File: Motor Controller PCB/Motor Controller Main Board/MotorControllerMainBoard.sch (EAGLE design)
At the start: 54 parts, among them T1 TEENSY_3.1_ALL_PINS, U1 TL072CDT

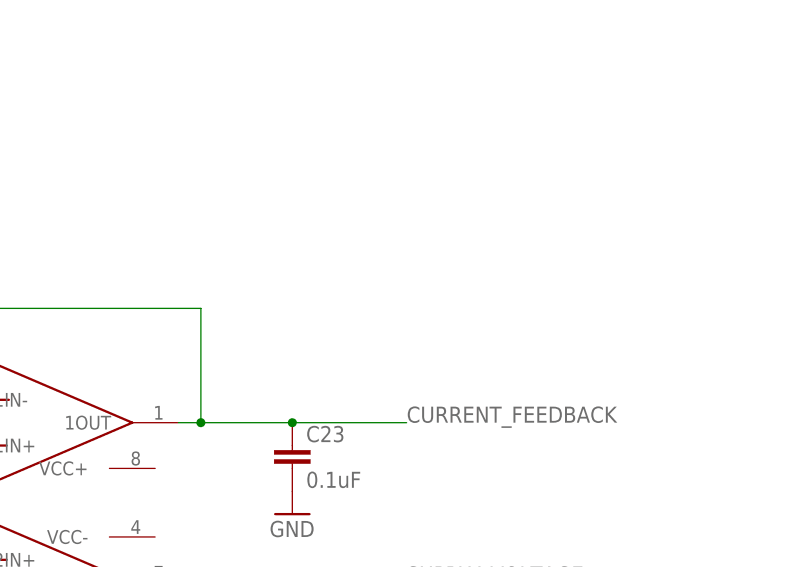
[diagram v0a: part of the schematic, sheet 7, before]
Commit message: Decided to use a different op-amp
A tad more expensive but this new op-amp selection offers little to no
current or voltage offset voltages.
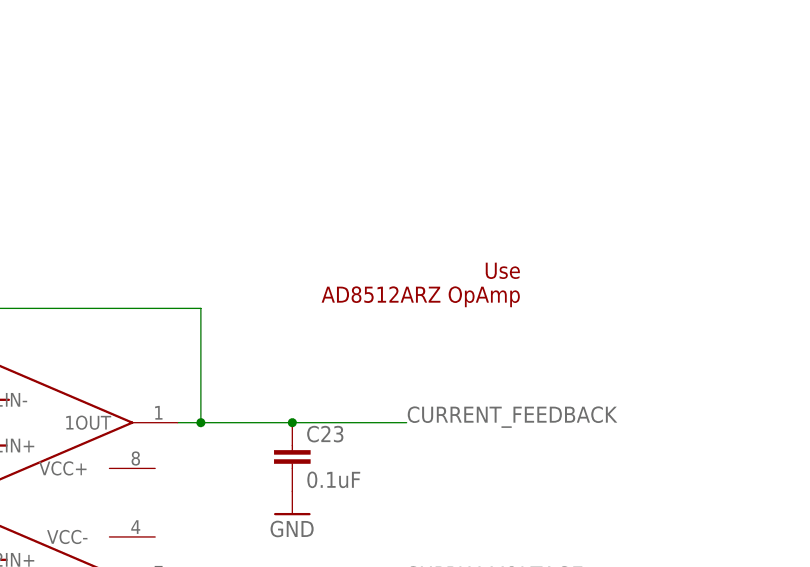
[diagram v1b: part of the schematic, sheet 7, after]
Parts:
- renumbered U1 to AD8512ARZ
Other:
- note added: "Use AD8512ARZ OpAmp"
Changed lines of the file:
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@@
 <part name="R4" library="SparkFun-Passives" deviceset="RESISTOR" device="0805-RES" value="3.3k"/>
 <part name="L1" library="SparkFun (2015_10_14 22_27_04 UTC)" deviceset="INDUCTOR" device="0805" value="42nH"/>
-<part name="U1" library="MotorControllerEagleLibrary" deviceset="TL072CDT" device=""/>
+<part name="AD8512ARZ" library="MotorControllerEagleLibrary" deviceset="TL072CDT" device=""/>
 <part name="C23" library="rcl" deviceset="C-EU" device="C0805" value="0.1uF"/>
 <part name="C24" library="rcl" deviceset="C-EU" device="C0805"/>
@@
 CONNECTIONS</text>
 <text x="195.58" y="43.18" size="1.778" layer="91">2OUT = (R7+R8)/(R5+R6)Vin =~ 1/10*Vin</text>
+<text x="238.76" y="96.52" size="1.778" layer="94" rot="R180">Use
+AD8512ARZ OpAmp
+</text>
 </plain>
 <instances>
@@
 <instance part="R3" gate="G$1" x="43.18" y="50.8" rot="R90"/>
 <instance part="R4" gate="G$1" x="83.82" y="50.8" rot="R90"/>
-<instance part="U1" gate="A" x="190.5" y="68.58"/>
+<instance part="AD8512ARZ" gate="A" x="190.5" y="68.58"/>
 <instance part="C23" gate="G$1" x="213.36" y="76.2"/>
 <instance part="C24" gate="G$1" x="294.64" y="76.2"/>
@@
 </segment>
 <segment>
-<pinref part="U1" gate="A" pin="1IN-"/>
+<pinref part="AD8512ARZ" gate="A" pin="1IN-"/>
 <wire x1="172.72" y1="81.28" x2="167.64" y2="81.28" width="0.1524" layer="91"/>
 <wire x1="167.64" y1="81.28" x2="167.64" y2="91.44" width="0.1524" layer="91"/>
 <wire x1="167.64" y1="91.44" x2="203.2" y2="91.44" width="0.1524" layer="91"/>
 <wire x1="203.2" y1="91.44" x2="203.2" y2="78.74" width="0.1524" layer="91"/>
-<pinref part="U1" gate="A" pin="1OUT"/>
+<pinref part="AD8512ARZ" gate="A" pin="1OUT"/>
 <wire x1="203.2" y1="78.74" x2="200.66" y2="78.74" width="0.1524" layer="91"/>
 <wire x1="203.2" y1="78.74" x2="213.36" y2="78.74" width="0.1524" layer="91"/>
@@
 <net name="CURRENT_SENSOR_OUTPUT" class="0">
 <segment>
-<pinref part="U1" gate="A" pin="1IN+"/>
+<pinref part="AD8512ARZ" gate="A" pin="1IN+"/>
 <wire x1="172.72" y1="76.2" x2="160.02" y2="76.2" width="0.1524" layer="91"/>
 <label x="142.24" y="76.2" size="1.778" layer="95"/>
@@
 <segment>
 <pinref part="R5" gate="G$1" pin="2"/>
-<pinref part="U1" gate="A" pin="2IN+"/>
+<pinref part="AD8512ARZ" gate="A" pin="2IN+"/>
 <wire x1="160.02" y1="66.04" x2="165.1" y2="63.5" width="0.1524" layer="91"/>
 <pinref part="R8" gate="G$1" pin="2"/>
@@
 <segment>
 <pinref part="R6" gate="G$1" pin="2"/>
-<pinref part="U1" gate="A" pin="2IN-"/>
+<pinref part="AD8512ARZ" gate="A" pin="2IN-"/>
 <wire x1="160.02" y1="55.88" x2="170.18" y2="58.42" width="0.1524" layer="91"/>
 <wire x1="170.18" y1="58.42" x2="172.72" y2="58.42" width="0.1524" layer="91"/>
@@
 <wire x1="187.96" y1="48.26" x2="203.2" y2="48.26" width="0.1524" layer="91"/>
 <wire x1="203.2" y1="48.26" x2="203.2" y2="60.96" width="0.1524" layer="91"/>
-<pinref part="U1" gate="A" pin="2OUT"/>
+<pinref part="AD8512ARZ" gate="A" pin="2OUT"/>
 <wire x1="203.2" y1="60.96" x2="200.66" y2="60.96" width="0.1524" layer="91"/>
 <wire x1="203.2" y1="60.96" x2="213.36" y2="60.96" width="0.1524" layer="91"/>

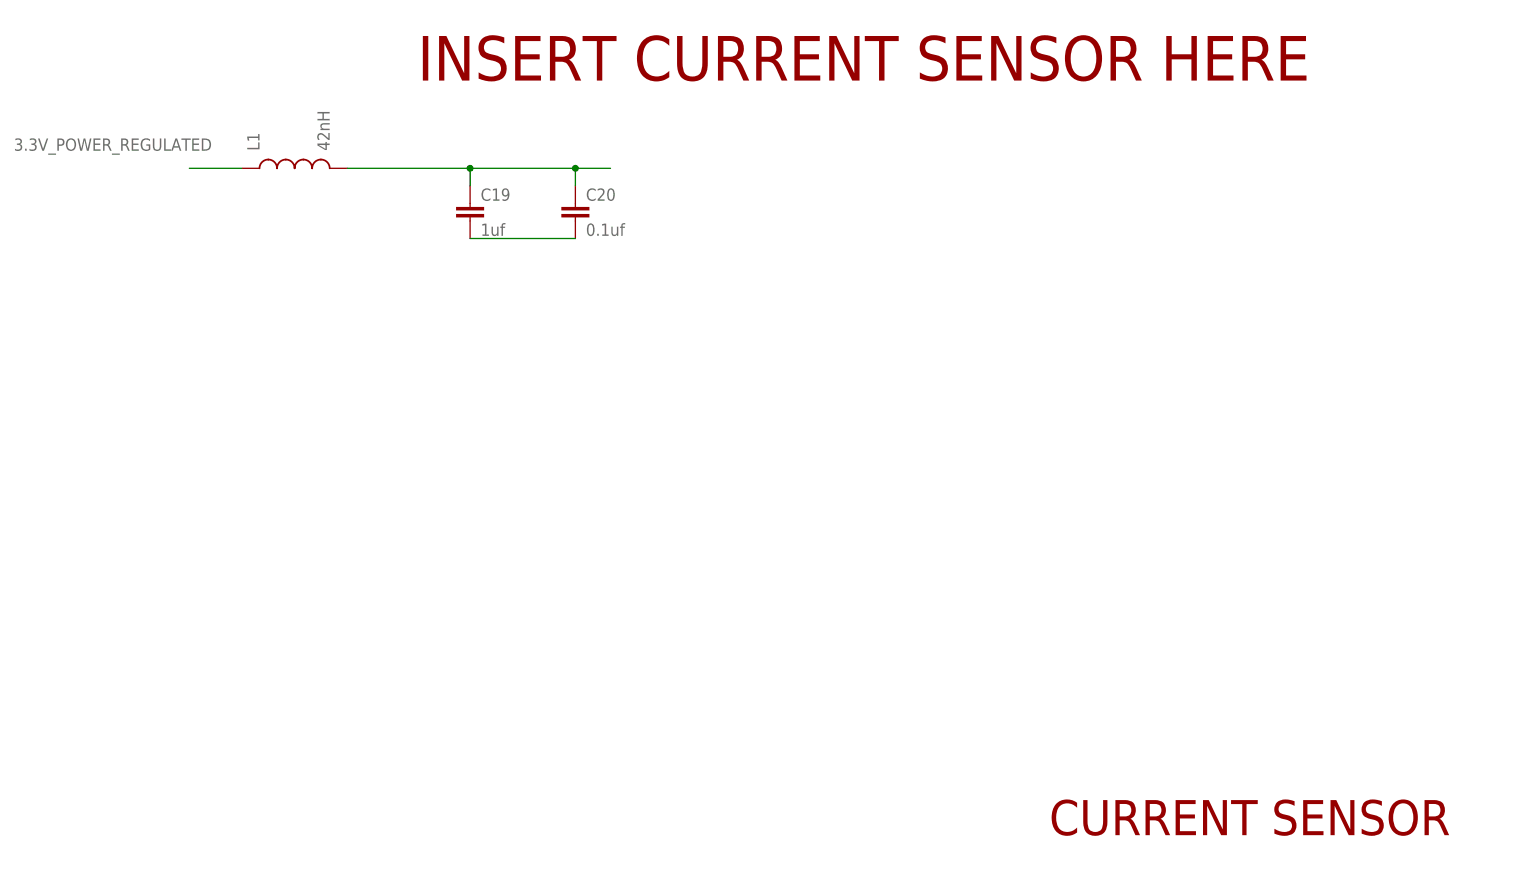
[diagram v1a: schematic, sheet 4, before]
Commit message: Implemented the Current Sensor on the Schematic
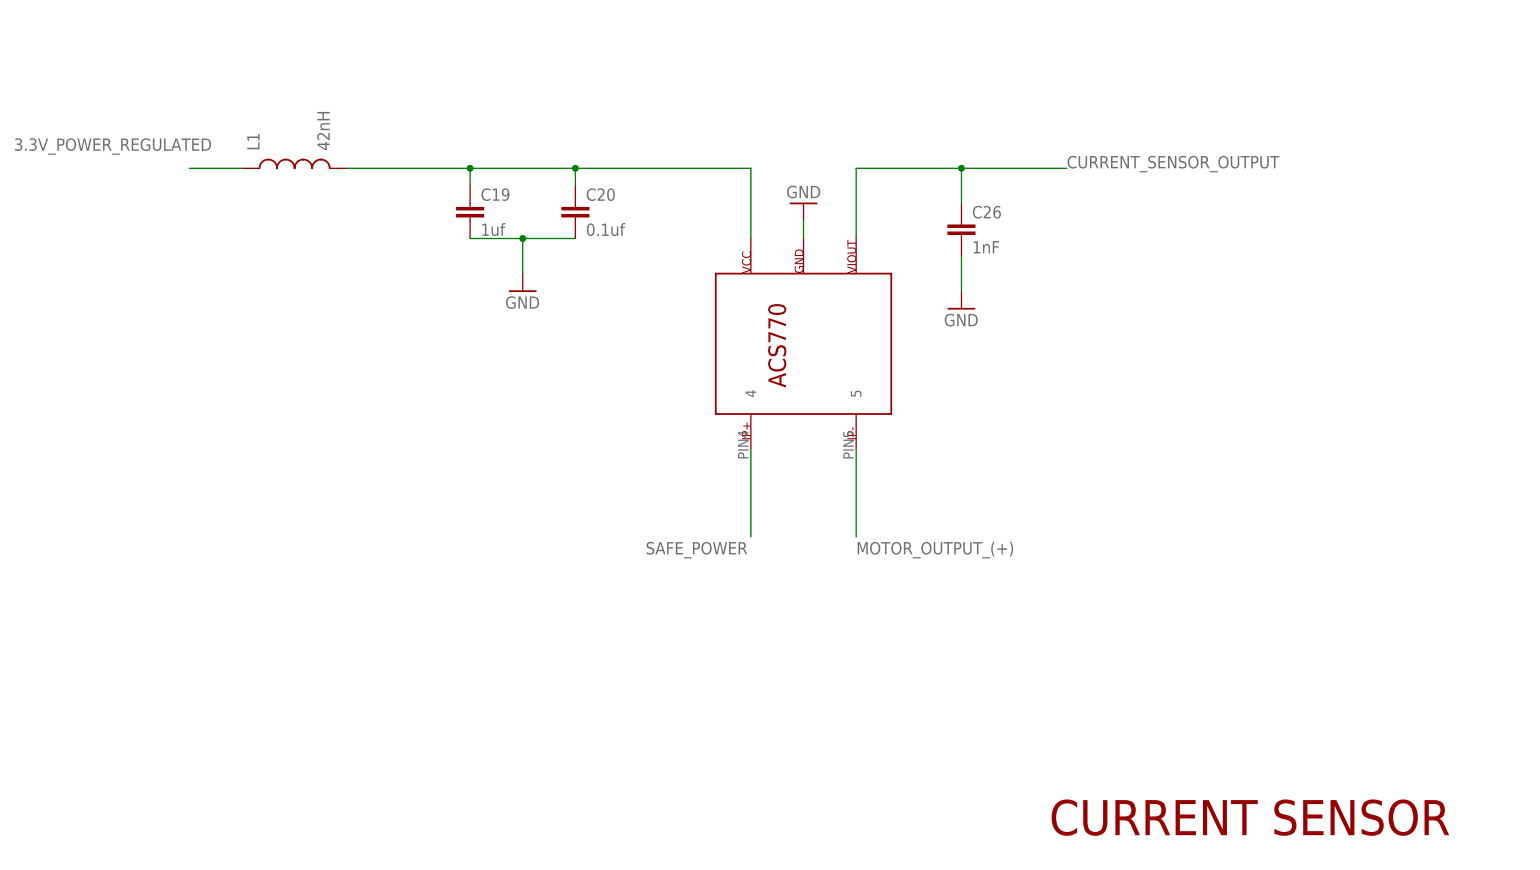
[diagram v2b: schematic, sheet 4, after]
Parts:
- added C26: 1nF, SparkFun-Capacitors:CAP0805
- added U$9: ACS770LCB_CURRENTSENSOR, ACS770 Current Sensor:ACS770LCB_CURRENTSENSOR
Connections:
- removed net N$2: C19.2, C20.2
- new net MOTOR_OUTPUT_(+): U$9.5
- net CURRENT_SENSOR_OUTPUT: now also C26.1, U$9.3
- net GND: now also C19.2, C20.2, C26.2, U$9.2
- net N$6: now also U$9.1
- net SAFE_POWER: now also U$9.4
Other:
- note removed: "INSERT CURRENT SENSOR HERE"
- moved on the sheet: R6

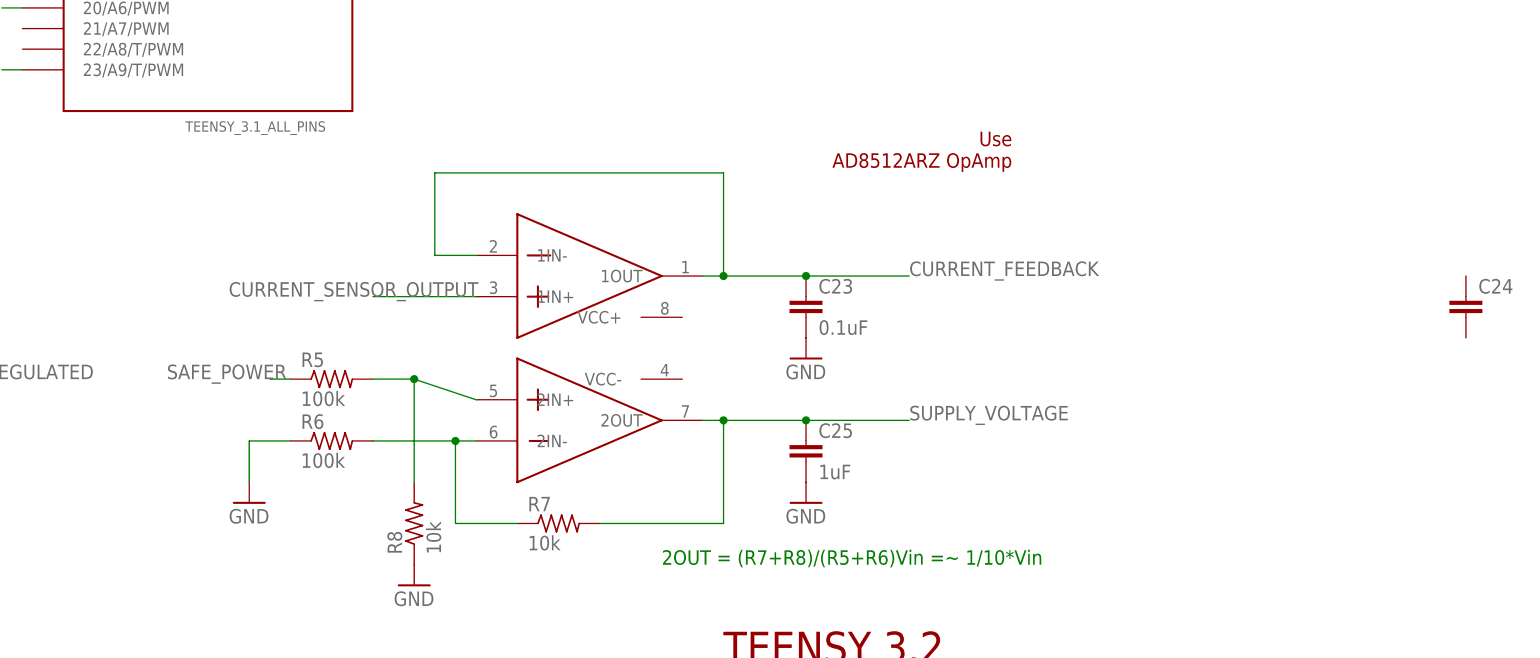
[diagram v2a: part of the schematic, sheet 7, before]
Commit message: Selected a cheaper op-amp
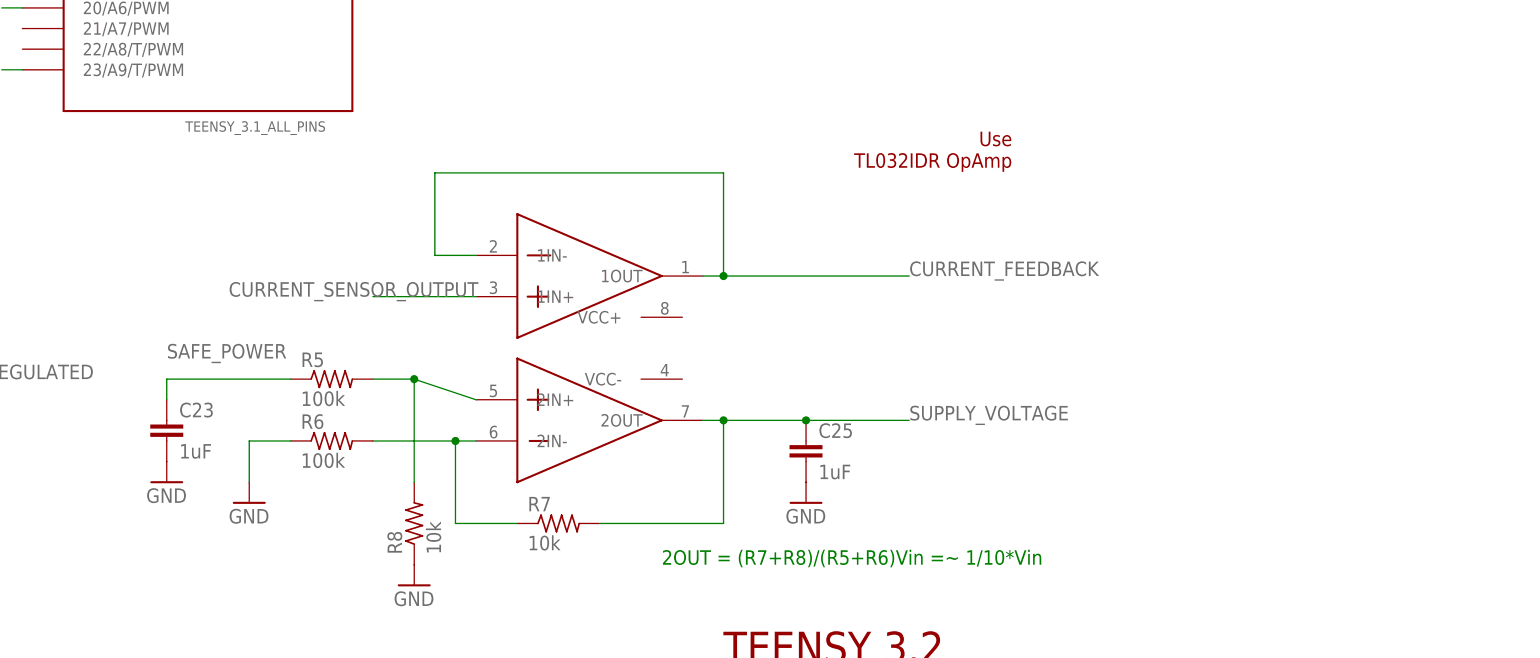
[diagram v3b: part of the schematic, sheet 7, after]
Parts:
- removed C24: (no value), rcl:C-EUC0805
- C23: value 0.1uF -> 1uF
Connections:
- net CURRENT_FEEDBACK: no longer C23.1
- net SAFE_POWER: now also C23.1
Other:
- note added: "Use TL032IDR OpAmp"
- note removed: "Use AD8512ARZ OpAmp"
- moved on the sheet: C23
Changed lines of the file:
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@@
 <part name="L1" library="SparkFun (2015_10_14 22_27_04 UTC)" deviceset="INDUCTOR" device="0805" value="42nH"/>
 <part name="AD8512ARZ" library="MotorControllerEagleLibrary" deviceset="TL072CDT" device=""/>
-<part name="C23" library="rcl" deviceset="C-EU" device="C0805" value="0.1uF"/>
-<part name="C24" library="rcl" deviceset="C-EU" device="C0805"/>
-<part name="GND9" library="E-P-008-R1.2" deviceset="GND" device=""/>
 <part name="R5" library="rcl" deviceset="R-US_" device="R0805" value="100k"/>
 <part name="R6" library="rcl" deviceset="R-US_" device="R0805" value="100k"/>
@@
 <part name="GND22" library="E-P-008-R1.2" deviceset="GND" device=""/>
 <part name="GND23" library="E-P-008-R1.2" deviceset="GND" device=""/>
+<part name="C23" library="rcl" deviceset="C-EU" device="C0805" value="1uF"/>
+<part name="GND9" library="E-P-008-R1.2" deviceset="GND" device=""/>
 </parts>
 <sheets>
@@
 <text x="195.58" y="43.18" size="1.778" layer="91">2OUT = (R7+R8)/(R5+R6)Vin =~ 1/10*Vin</text>
 <text x="238.76" y="96.52" size="1.778" layer="94" rot="R180">Use
-AD8512ARZ OpAmp
+TL032IDR OpAmp
 </text>
 </plain>
@@
 <instance part="R4" gate="G$1" x="83.82" y="50.8" rot="R90"/>
 <instance part="AD8512ARZ" gate="A" x="190.5" y="68.58"/>
-<instance part="C23" gate="G$1" x="213.36" y="76.2"/>
-<instance part="C24" gate="G$1" x="294.64" y="76.2"/>
-<instance part="GND9" gate="1" x="213.36" y="68.58"/>
 <instance part="R5" gate="G$1" x="154.94" y="66.04"/>
 <instance part="R6" gate="G$1" x="154.94" y="58.42"/>
@@
 <instance part="GND11" gate="1" x="213.36" y="50.8"/>
 <instance part="GND12" gate="1" x="144.78" y="50.8"/>
+<instance part="C23" gate="G$1" x="134.62" y="60.96"/>
+<instance part="GND9" gate="1" x="134.62" y="53.34"/>
 </instances>
 <busses>
@@
 </segment>
 <segment>
-<pinref part="C23" gate="G$1" pin="2"/>
-<pinref part="GND9" gate="1" pin="GND"/>
-</segment>
-<segment>
 <pinref part="R8" gate="G$1" pin="1"/>
 <pinref part="GND10" gate="1" pin="GND"/>
@@
 <wire x1="149.86" y1="58.42" x2="144.78" y2="58.42" width="0.1524" layer="91"/>
 <wire x1="144.78" y1="58.42" x2="144.78" y2="53.34" width="0.1524" layer="91"/>
+</segment>
+<segment>
+<pinref part="C23" gate="G$1" pin="2"/>
+<pinref part="GND9" gate="1" pin="GND"/>
 </segment>
 </net>
@@
 <pinref part="AD8512ARZ" gate="A" pin="1OUT"/>
 <wire x1="203.2" y1="78.74" x2="200.66" y2="78.74" width="0.1524" layer="91"/>
-<wire x1="203.2" y1="78.74" x2="213.36" y2="78.74" width="0.1524" layer="91"/>
 <junction x="203.2" y="78.74"/>
-<pinref part="C23" gate="G$1" pin="1"/>
-<junction x="213.36" y="78.74"/>
-<wire x1="213.36" y1="78.74" x2="226.06" y2="78.74" width="0.1524" layer="91"/>
+<wire x1="203.2" y1="78.74" x2="226.06" y2="78.74" width="0.1524" layer="91"/>
 <label x="226.06" y="78.74" size="1.778" layer="95"/>
 </segment>
@@
 <segment>
 <pinref part="R5" gate="G$1" pin="1"/>
-<wire x1="149.86" y1="66.04" x2="147.32" y2="66.04" width="0.1524" layer="91"/>
-<label x="134.62" y="66.04" size="1.778" layer="95"/>
-</segment>
-</net>
+<label x="134.62" y="68.58" size="1.778" layer="95"/>
+<pinref part="C23" gate="G$1" pin="1"/>
+<wire x1="134.62" y1="63.5" x2="134.62" y2="66.04" width="0.1524" layer="91"/>
+<wire x1="134.62" y1="66.04" x2="149.86" y2="66.04" width="0.1524" layer="91"/>
+</segment>
+</net>
